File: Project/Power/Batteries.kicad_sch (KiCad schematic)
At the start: 52 parts, among them J10 Battery, J11 Battery, J12 Battery, J9 Battery, Q3 SQJ138ELP, Q4 SQJ138ELP, Q5 SQJ138ELP, Q6 SQJ138ELP, U10 INA199B3DCKR, U11 TL331, U12 INA199B3DCKR, U13 TL331, U2 NCV68061, U3 NCV68061, U4 INA199B3DCKR, U5 TL331, U6 INA199B3DCKR, U7 TL331, U8 NCV68061, U9 NCV68061

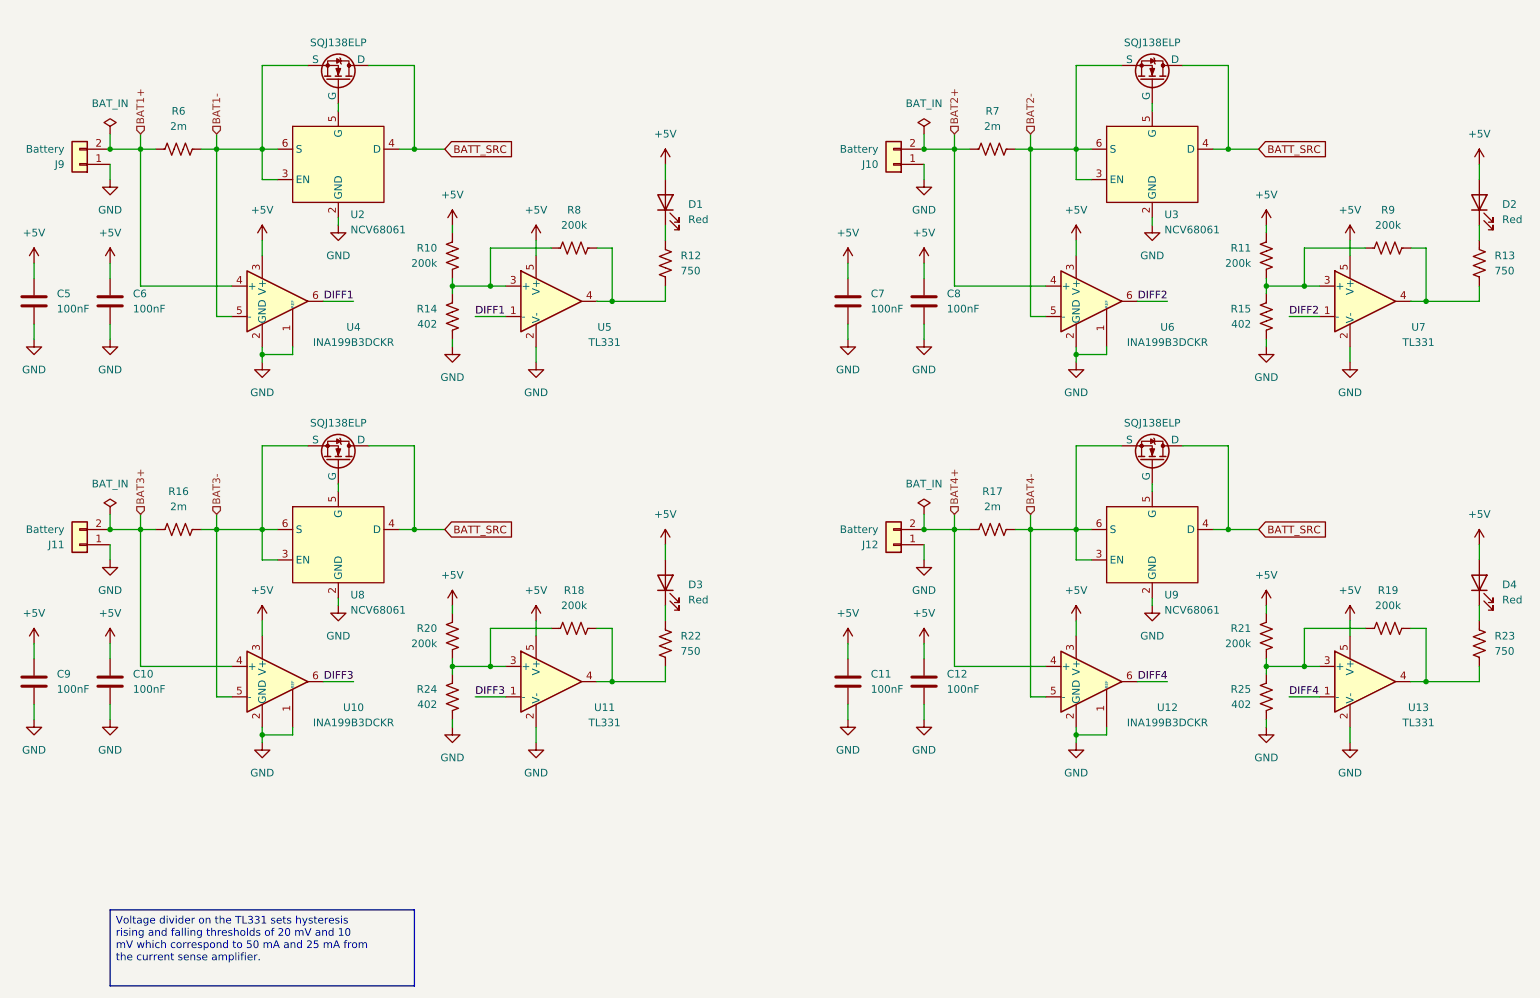
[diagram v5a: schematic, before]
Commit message: Add capacitors to ideal diode inputs / outputs
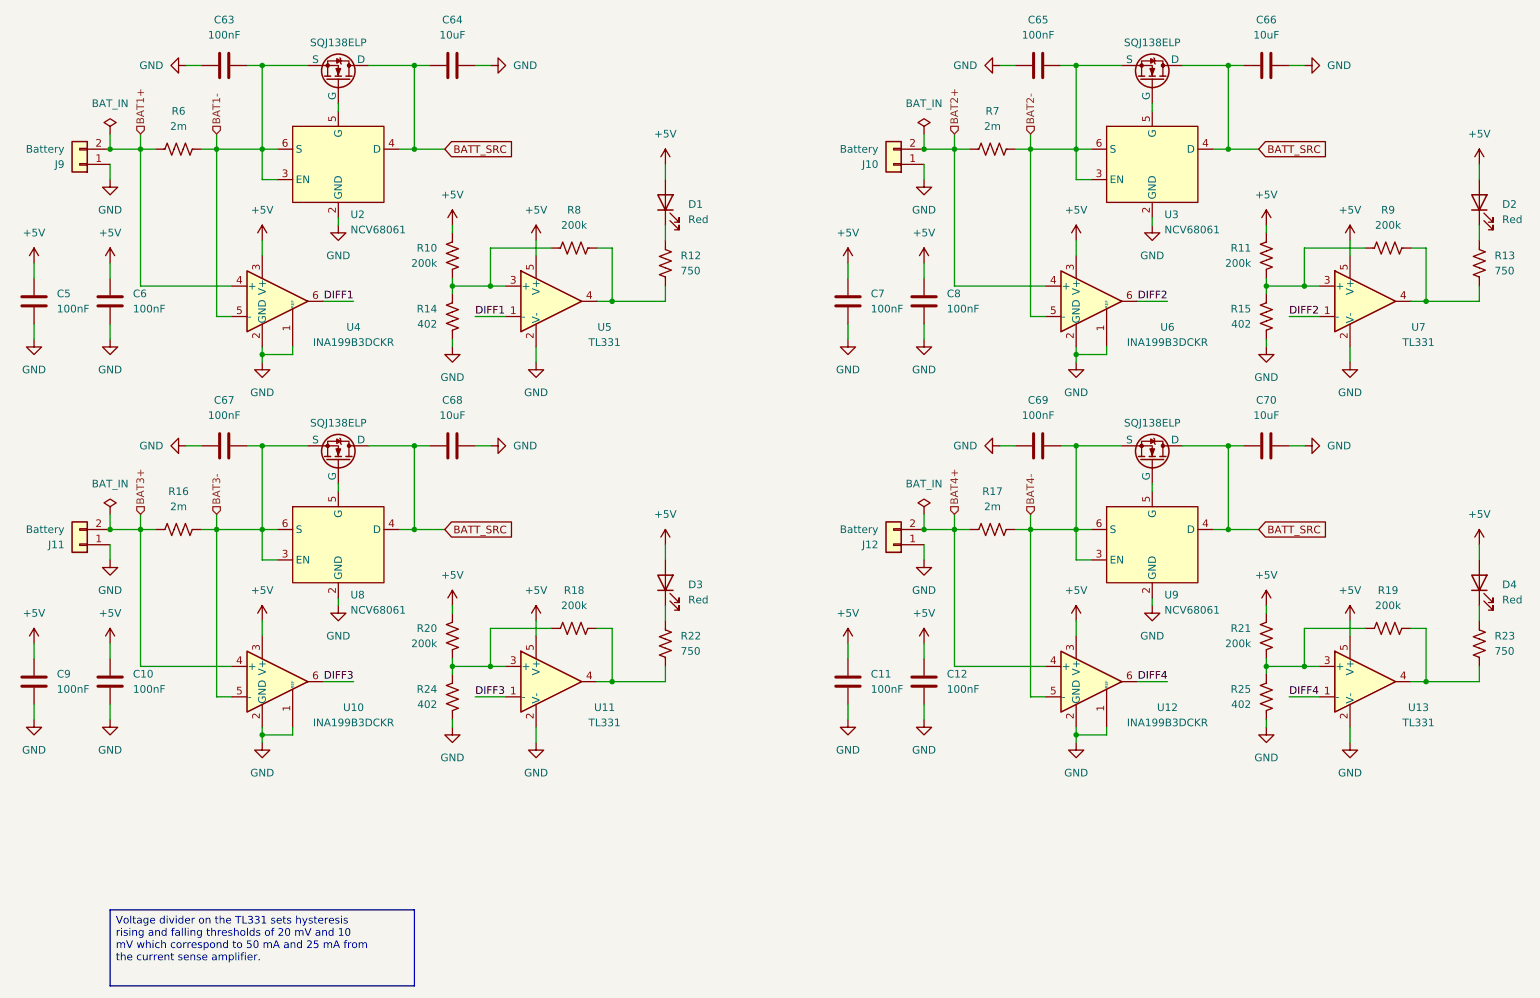
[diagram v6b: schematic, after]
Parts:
- added C63, C65, C67, C69: 100nF, Capacitor_SMD:C_0603_1608Metric, symbol Device:C
- added C64, C66, C68, C70: 10uF, Capacitor_SMD:C_1206_3216Metric, symbol Device:C
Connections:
- net BAT1-: now also C63.2
- net BAT2-: now also C65.2
- net BAT3-: now also C67.2
- net BAT4-: now also C69.2
- net BATT_SRC: now also C64.1, C66.1, C68.1, C70.1
- net GND: now also C63.1, C64.2, C65.1, C66.2, C67.1, C68.2, C69.1, C70.2

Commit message: Change connectors to vertical
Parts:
- J10, J11, J12, J9: footprint Connector_AMASS:AMASS_XT60PW-M_1x02_P7.20mm_Horizontal -> Connector_AMASS:AMASS_XT60-M_1x02_P7.20mm_Vertical; Listing https://www.lcsc.com/product-detail/C98732.html -> https://www.sparkfun.com/xt60-connectors-male-female-pair.h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
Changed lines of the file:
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@@
 			)
 		)
-		(property "Footprint" "Connector_AMASS:AMASS_XT60PW-M_1x02_P7.20mm_Horizontal"
+		(property "Footprint" "Connector_AMASS:AMASS_XT60-M_1x02_P7.20mm_Vertical"
 			(at 168.91 40.64 0)
 			(effects
@@
 			)
 		)
-		(property "Datasheet" "https://www.lcsc.com/datasheet/C98732.pdf"
+		(property "Datasheet" "https://cdn.sparkfun.com/datasheets/Prototyping/xt60.pdf"
 			(at 168.91 40.64 0)
 			(effects
@@
 			)
 		)
-		(property "Listing" "https://www.lcsc.com/product-detail/C98732.html"
+		(property "Listing" "https://www.sparkfun.com/xt60-connectors-male-female-pair.html"
 			(at 168.91 40.64 0)
 			(effects
@@
 			)
 		)
-		(property "Footprint" "Connector_AMASS:AMASS_XT60PW-M_1x02_P7.20mm_Horizontal"
+		(property "Footprint" "Connector_AMASS:AMASS_XT60-M_1x02_P7.20mm_Vertical"
 			(at 168.91 104.14 0)
 			(effects
@@
 			)
 		)
-		(property "Datasheet" "https://www.lcsc.com/datasheet/C98732.pdf"
+		(property "Datasheet" "https://cdn.sparkfun.com/datasheets/Prototyping/xt60.pdf"
 			(at 168.91 104.14 0)
 			(effects
@@
 			)
 		)
-		(property "Listing" "https://www.lcsc.com/product-detail/C98732.html"
+		(property "Listing" "https://www.sparkfun.com/xt60-connectors-male-female-pair.html"
 			(at 168.91 104.14 0)
 			(effects
@@
 			)
 		)
-		(property "Footprint" "Connector_AMASS:AMASS_XT60PW-M_1x02_P7.20mm_Horizontal"
+		(property "Footprint" "Connector_AMASS:AMASS_XT60-M_1x02_P7.20mm_Vertical"
 			(at 33.02 104.14 0)
 			(effects
@@
 			)
 		)
-		(property "Datasheet" "https://www.lcsc.com/datasheet/C98732.pdf"
+		(property "Datasheet" "https://cdn.sparkfun.com/datasheets/Prototyping/xt60.pdf"
 			(at 33.02 104.14 0)
 			(effects
@@
 			)
 		)
-		(property "Listing" "https://www.lcsc.com/product-detail/C98732.html"
+		(property "Listing" "https://www.sparkfun.com/xt60-connectors-male-female-pair.html"
 			(at 33.02 104.14 0)
 			(effects
@@
 			)
 		)
-		(property "Footprint" "Connector_AMASS:AMASS_XT60PW-M_1x02_P7.20mm_Horizontal"
+		(property "Footprint" "Connector_AMASS:AMASS_XT60-M_1x02_P7.20mm_Vertical"
 			(at 33.02 40.64 0)
 			(effects
@@
 			)
 		)
-		(property "Datasheet" "https://www.lcsc.com/datasheet/C98732.pdf"
+		(property "Datasheet" "https://cdn.sparkfun.com/datasheets/Prototyping/xt60.pdf"
 			(at 33.02 40.64 0)
 			(effects
@@
 			)
 		)
-		(property "Listing" "https://www.lcsc.com/product-detail/C98732.html"
+		(property "Listing" "https://www.sparkfun.com/xt60-connectors-male-female-pair.html"
 			(at 33.02 40.64 0)
 			(effects
